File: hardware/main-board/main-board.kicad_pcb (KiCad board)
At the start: 2 copper layers, 39.5 x 80.5 mm, 58 parts, among them J14 Top Left(M), J16 Top Right (M), J18 Bottom Left(M), J20 Bottom Right(M), J9 PWR, Q1 MMBFJ201, U1 TL074, U2 AS3340, U3 79L05, U4 LP2950

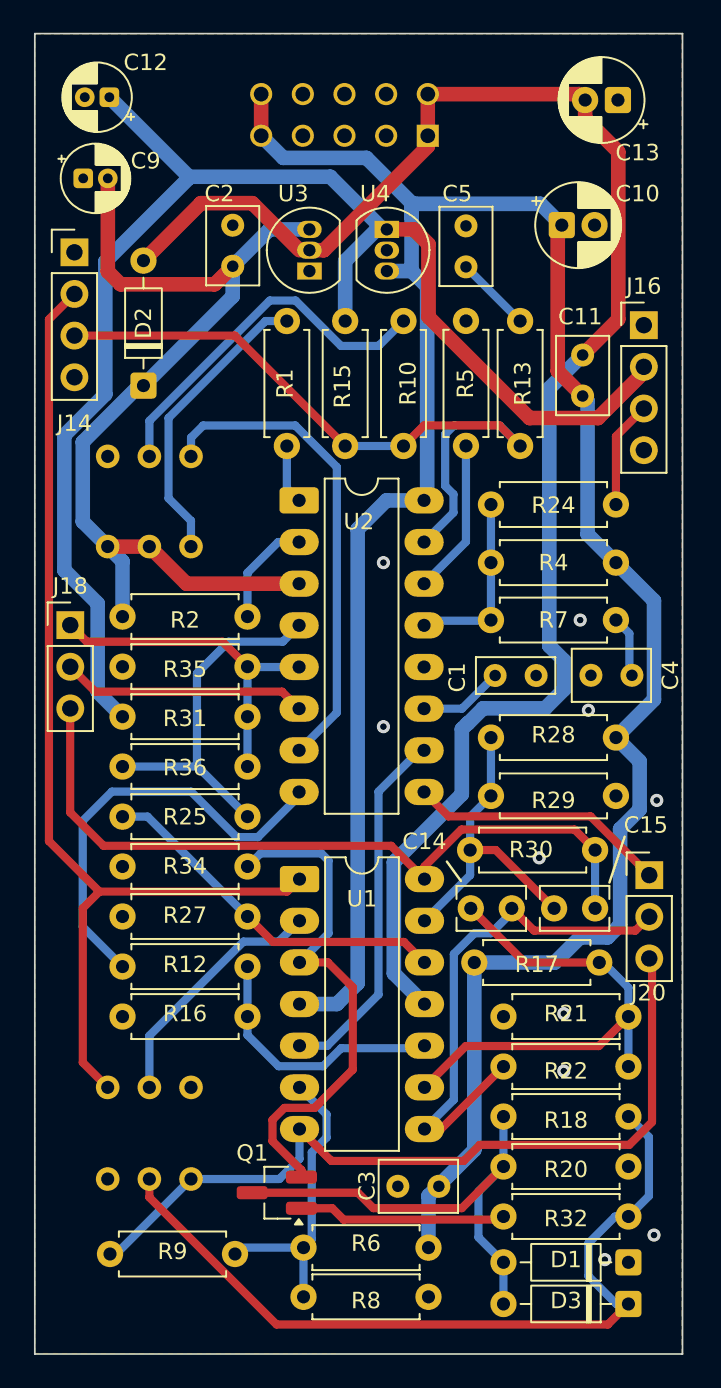
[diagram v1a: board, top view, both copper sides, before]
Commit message: feature: improve docs + front panel design
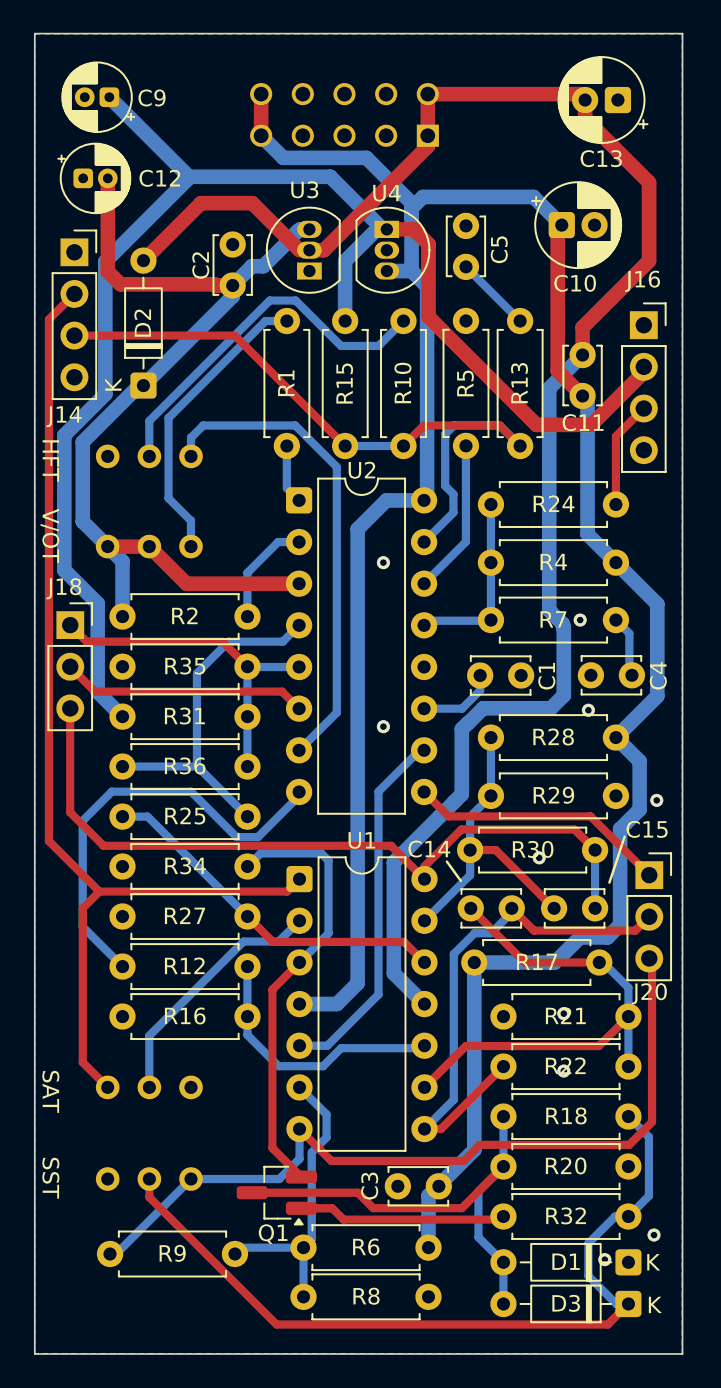
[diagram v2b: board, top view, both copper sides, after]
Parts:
- C1: footprint Capacitor_THT:C_Rect_L4.6mm_W2.0mm_P2.50mm_MKS02_FKP02 -> Eurorack Common:C_Disc_D3.4mm_W2.1mm_P2.50mm
- C10, C13: footprint Capacitor_THT:CP_Radial_D5.0mm_P2.00mm -> Eurorack Common:CP_Radial_D5.0mm_H11.0mm_P2.00mm
- C11, C2, C3, C4, C5: footprint Capacitor_THT:C_Rect_L4.6mm_W3.0mm_P2.50mm_MKS02_FKP02 -> Eurorack Common:C_Disc_D3.4mm_W2.1mm_P2.50mm
- C12, C9: footprint Capacitor_THT:CP_Radial_D4.0mm_P1.50mm -> Eurorack Common:CP_Radial_D4.0mm_P1.50mm
- C14, C15: footprint Capacitor_THT:C_Rect_L4.0mm_W2.5mm_P2.50mm -> Eurorack Common:C_Disc_D3.4mm_W2.1mm_P2.50mm
- D1, D2, D3: value 1N4148 -> ~; footprint Diode_THT:D_DO-35_SOD27_P7.62mm_Horizontal -> Eurorack Common:D_DO-35_SOD27_P7.62mm_Horizontal
- J14: value Top Left(M) -> ~; footprint Connector_PinHeader_2.54mm:PinHeader_1x04_P2.54mm_Vertical -> Eurorack Common:PinSocket_1x04_P2.54mm_Vertical
- J16: value Top Right (M) -> ~; footprint Connector_PinHeader_2.54mm:PinHeader_1x04_P2.54mm_Vertical -> Eurorack Common:PinSocket_1x04_P2.54mm_Vertical
- J18: value Bottom Left(M) -> ~; footprint Connector_PinHeader_2.54mm:PinHeader_1x03_P2.54mm_Vertical -> Eurorack Common:PinSocket_1x03_P2.54mm_Vertical
- J20: value Bottom Right(M) -> ~; footprint Connector_PinHeader_2.54mm:PinHeader_1x03_P2.54mm_Vertical -> Eurorack Common:PinSocket_1x03_P2.54mm_Vertical
- J9: value PWR -> ~
- Q1: footprint Package_TO_SOT_SMD:SOT-23_Handsoldering -> Eurorack Common:SOT-23_Handsoldering
- R1, R10, R12, R13, R15, R16, R17, R18, R2, R20, R21, R22, R24, R25, R27, R28, R29, R30, R31, R32, R34, R35, R36, R4, R5, R6, R7, R8, R9: footprint Resistor_THT:R_Axial_DIN0207_L6.3mm_D2.5mm_P7.62mm_Horizontal -> Eurorack Common:R_Axial_DIN0207_L6.3mm_D2.5mm_P7.62mm_Horizontal
- RV1, RV2, RV6, RV7: footprint Potentiometer_THT:Potentiometer_Bourns_3296W_Vertical -> Eurorack Common:Potentiometer_Bourns_3296W_Vertical
- U1: footprint Package_DIP:DIP-14_W7.62mm_LongPads -> Eurorack Common:DIP-14_W7.62mm
- U2: footprint Package_DIP:DIP-16_W7.62mm_LongPads -> Eurorack Common:DIP-16_W7.62mm
- U3, U4: footprint Package_TO_SOT_THT:TO-92_Inline -> Eurorack Common:TO-92_Inline
- moved C2 1.18 mm to (27.3, 28.1)
- moved C1 0.91 mm to (42.4, 54.4)
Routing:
- net Net-(U1A-+): track 31.7 -> 26.9 mm
- net -12VA: track 100.3 -> 102.1 mm
- net -5VA: track 58.6 -> 57.5 mm
- net +12VA: track 156.0 -> 156.5 mm
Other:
- board text added: "HFT"
- board text added: "SAT"
- board text added: "SST"
- board text added: "V/OT"
